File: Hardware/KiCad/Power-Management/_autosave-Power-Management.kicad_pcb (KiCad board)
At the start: 2 copper layers, 108 x 67 mm, 52 parts, among them IC1 RT9080-33GJ5, J1 Screw_Terminal_01x02, J2 Conn_01x06, J3 Screw_Terminal_01x02, K1 FINDER-36.11, Q1 BC817, T1 ZMPT101B, U1 STM32F401CCU6, U2 ACS758xCB-050B-PFF, U3 ESP-01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

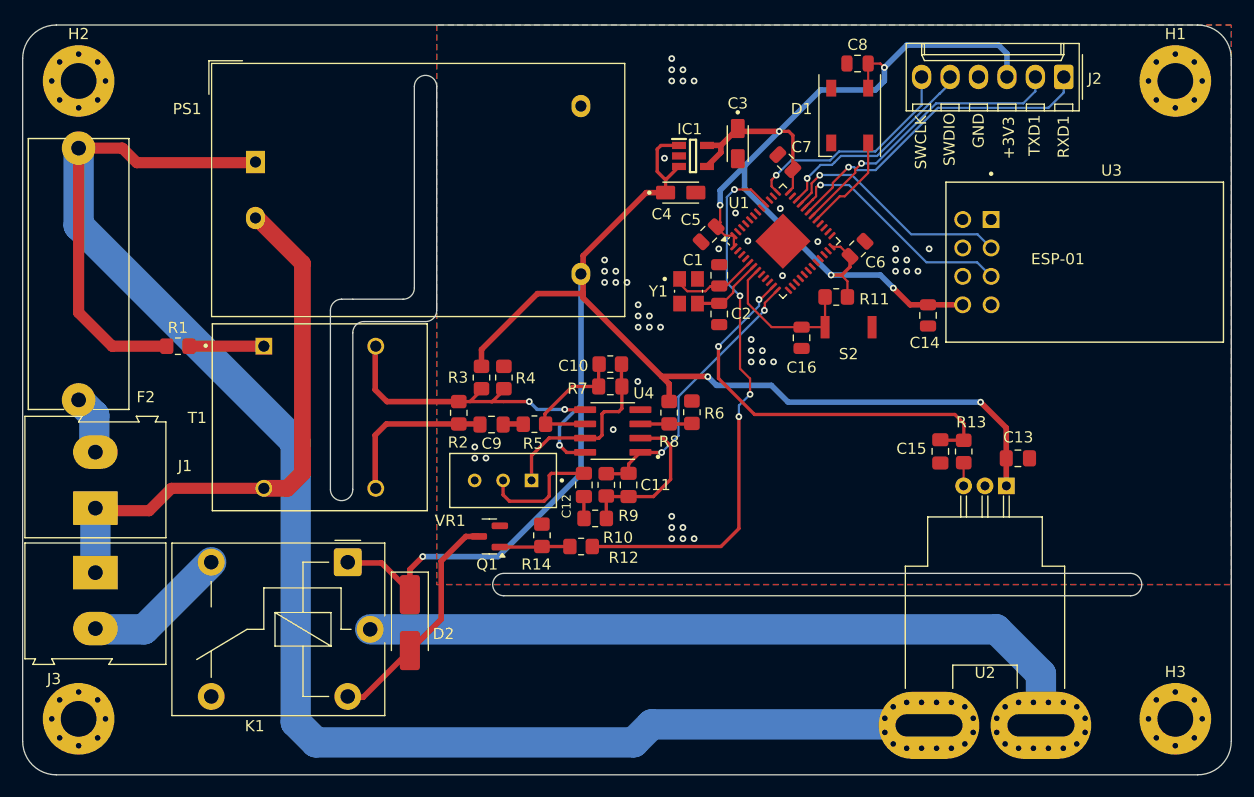
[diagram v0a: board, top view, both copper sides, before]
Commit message: refactor: exchange of STMF401 for F103
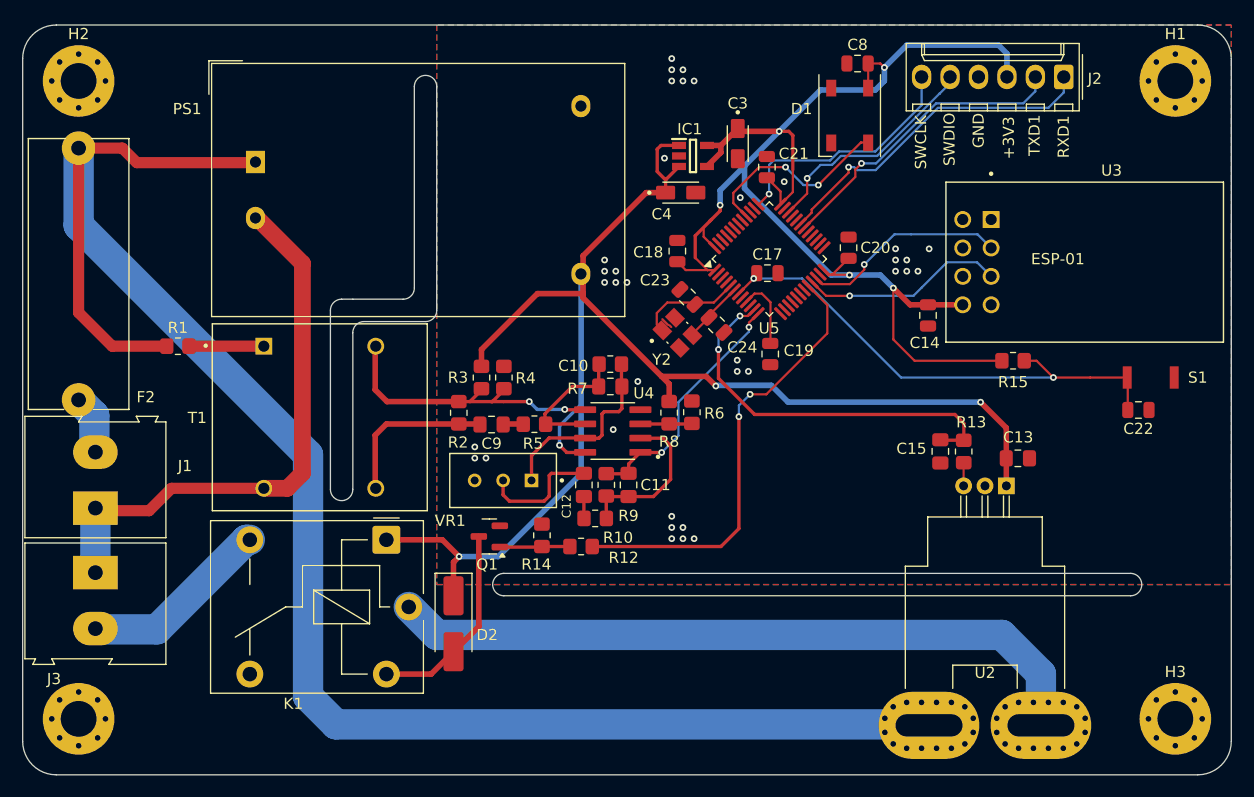
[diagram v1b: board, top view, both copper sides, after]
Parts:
- removed C1: 5pF, Capacitor_SMD:C_0805_2012Metric
- removed C16, C6: 100nF, Capacitor_SMD:C_0805_2012Metric
- removed C2, C7: 10pF, Capacitor_SMD:C_0805_2012Metric
- removed C5: 22uF 10V, Capacitor_SMD:C_0805_2012Metric
- removed R11: 10K, Resistor_SMD:R_0805_2012Metric_Pad1.20x1.40mm_HandSolder
- removed S2: SKRKAEE010, SKRKAEE010:SKRK
- removed U1: STM32F401CCU6, Package_DFN_QFN:QFN-48-1EP_7x7mm_P0.5mm_EP3.5x3.5mm
- removed Y1: 25Mhz, TSX-3225_25.0000MF10Z-W:XTAL_TSX-3225_25.0000MF10Z-W
- added C17: 100nF, Capacitor_SMD:C_0805_2012Metric, F.Cu at (188.6, 72.2)
- added C18: 100nF, Capacitor_SMD:C_0805_2012Metric, F.Cu at (180.5, 70.2)
- added C19: 10uF, Capacitor_SMD:C_0805_2012Metric, F.Cu at (188.8, 79.4)
- added C20: 100nF, Capacitor_SMD:C_0805_2012Metric, F.Cu at (195.8, 69.9)
- added C21: 100nF, Capacitor_SMD:C_0805_2012Metric, F.Cu at (188.5, 62.7)
- added C22: 100nF, Capacitor_SMD:C_0805_2012Metric, F.Cu at (221.7, 84.4)
- added C23: 10pF, Capacitor_SMD:C_0805_2012Metric, F.Cu at (181.4, 74.3)
- added C24: 10pF, Capacitor_SMD:C_0805_2012Metric, F.Cu at (184.0, 76.8)
- added R15: 10K, Resistor_SMD:R_0805_2012Metric_Pad1.20x1.40mm_HandSolder, F.Cu at (210.5, 80.0)
- added S1: SKRKAEE010, SKRKAEE010:SKRK, F.Cu at (222.8, 81.5)
- added U5: STM32F103C8Tx, Package_QFP:LQFP-48_7x7mm_P0.5mm, F.Cu at (188.7, 70.9)
- added Y2: 16Mhz, TSX-3225_25.0000MF10Z-W:XTAL_TSX-3225_25.0000MF10Z-W, F.Cu at (180.5, 77.5)
- moved K1 3.99 mm to (154.5, 96.0)
- moved D2 3.90 mm to (160.5, 103.5)
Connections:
- U3 pad 2: RXD6 -> RXD3
- U3 pad 3: TXD6 -> TXD3
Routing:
- net Net-(U5-NRST): track 0.00 -> 45.1 mm, vias 0 -> 2
- net +3V3: track 92.9 -> 124.1 mm
- net TXD6: track 21.5 -> 0.00 mm, vias 1 -> 0
- net RXD6: track 21.3 -> 0.00 mm, vias 1 -> 0
- net RXD3: track 0.00 -> 18.5 mm, vias 0 -> 1
- net TXD3: track 0.00 -> 18.3 mm, vias 0 -> 1
- net Net-(U1-NRST): track 13.8 -> 0.00 mm
- net Net-(U5-PD0): track 0.00 -> 9.22 mm
- net PIN_LED_RGB: track 9.06 -> 17.8 mm, vias 0 -> 2
- net PIN_RELAY: track 48.9 -> 40.3 mm, vias 4 -> 2
- net Net-(U1-PH0): track 8.00 -> 0.00 mm
- net Net-(U1-PH1): track 6.68 -> 0.00 mm
- net F/N-1 Borne: track 12.9 -> 17.1 mm
- net Net-(U5-PD1): track 0.00 -> 4.19 mm
- net +5V: track 137.3 -> 133.5 mm
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
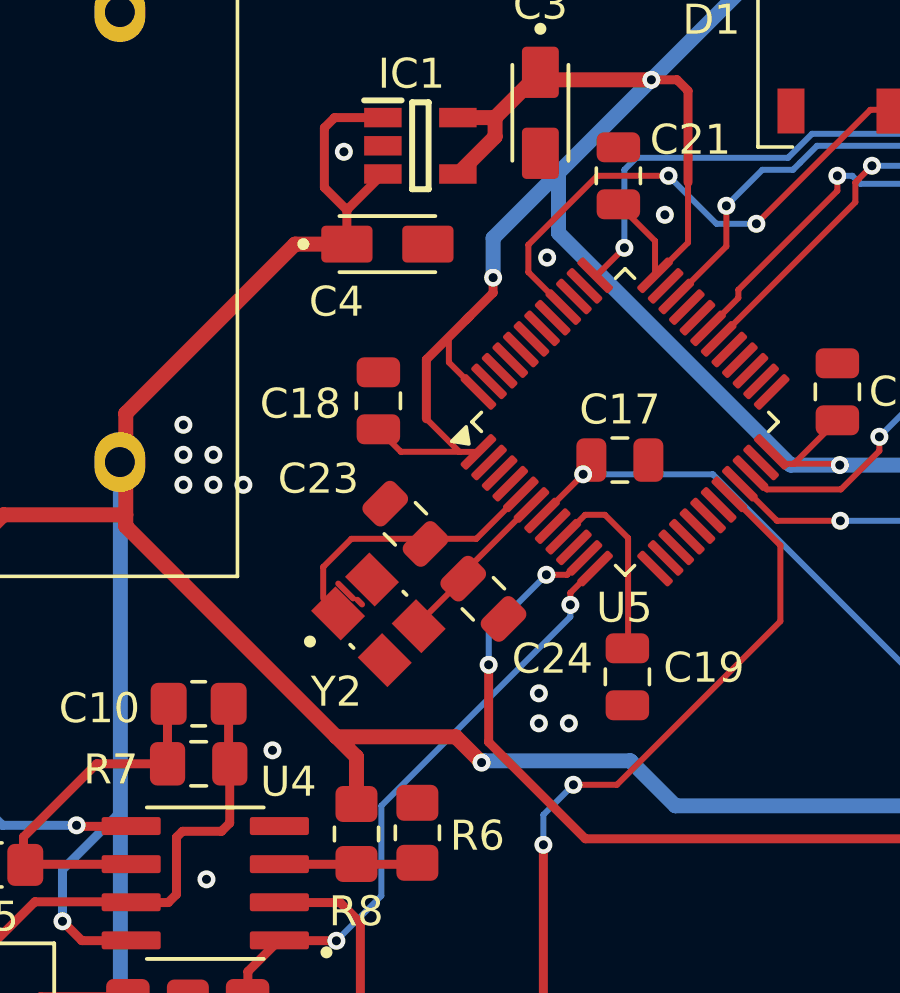
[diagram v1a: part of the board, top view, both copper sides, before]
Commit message: feat: footprint and step
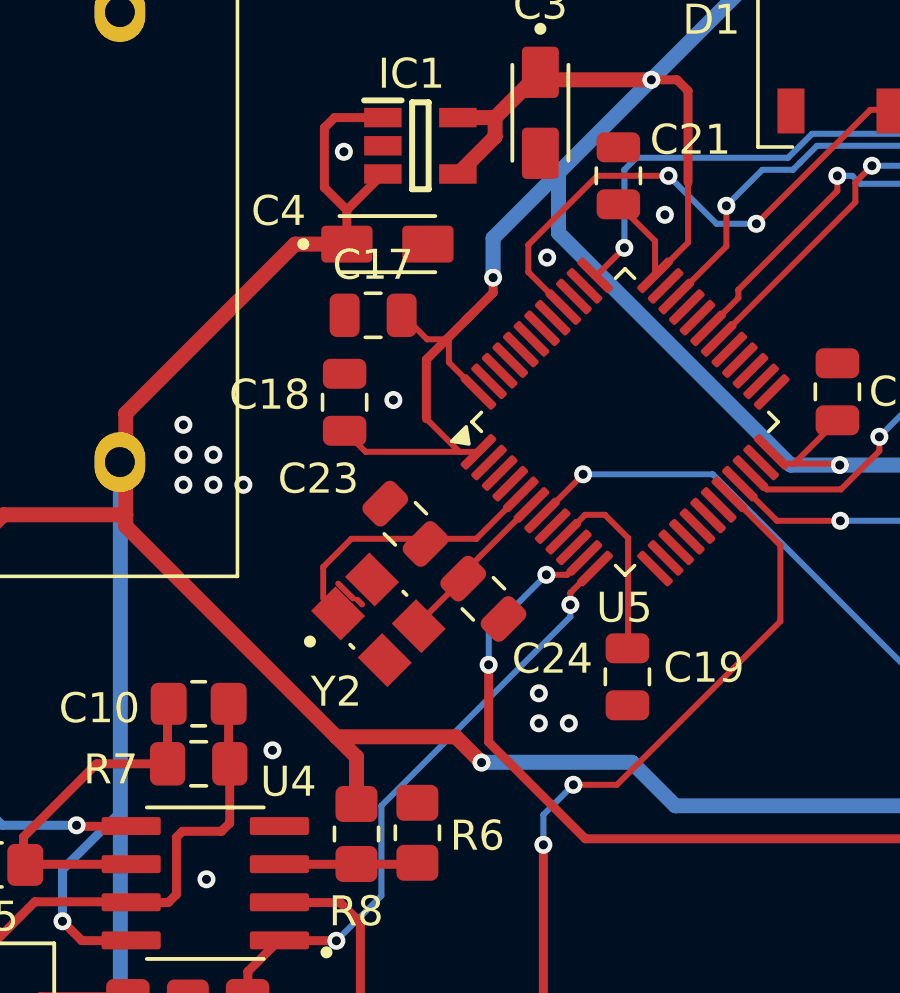
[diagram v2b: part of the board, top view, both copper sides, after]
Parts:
- moved C17 9.54 mm to (180.3, 67.3)
- moved C18 1.13 mm to (179.4, 70.2)
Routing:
- net +3V3: track 124.1 -> 127.0 mm
- net GND: vias 36 -> 37
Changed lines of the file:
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@@
 		(at 180.8 64.977)
 		(property "Reference" "C4"
-			(at -1.7 1.923 0)
+			(at -3.625 -1.102 0)
 			(layer "F.SilkS")
 			(effects
@@
 	(footprint "Capacitor_SMD:C_0805_2012Metric"
 		(layer "F.Cu")
-		(at 188.55 72.175)
+		(at 180.325 67.35)
 		(descr "Capacitor SMD 0805 (2012 Metric), square (rectangular) end terminal, IPC_7351 nominal, (Body size source: IPC-SM-782 page 76, https://www.pcb-3d.com/wordpress/wp-content/uploads/ipc-sm-782a_amendment_1_and_2.pdf, https://docs.google.com/spreadsheets/d/1BsfQQcO9C6DZCsRaXUlFlo91Tg2WpOkGARC1WS5S8t0/edit?usp=sharing), generated with kicad-footprint-generator")
 		(tags "capacitor")
@@
 	(footprint "Capacitor_SMD:C_0805_2012Metric"
 		(layer "F.Cu")
-		(at 180.5 70.2 -90)
+		(at 179.375 70.25 -90)
 		(descr "Capacitor SMD 0805 (2012 Metric), square (rectangular) end terminal, IPC_7351 nominal, (Body size source: IPC-SM-782 page 76, https://www.pcb-3d.com/wordpress/wp-content/uploads/ipc-sm-782a_amendment_1_and_2.pdf, https://docs.google.com/spreadsheets/d/1BsfQQcO9C6DZCsRaXUlFlo91Tg2WpOkGARC1WS5S8t0/edit?usp=sharing), generated with kicad-footprint-generator")
 		(tags "capacitor")
 		(property "Reference" "C18"
-			(at 0.1 2.6 180)
+			(at -0.25 2.5 180)
 			(layer "F.SilkS")
 			(effects
@@
 	)
 	(via
+		(at 181 70.175)
+		(size 0.6)
+		(drill 0.3)
+		(layers "F.Cu" "B.Cu")
+		(free yes)
+		(net 1)
+	)
+	(via
 		(at 180 94.9)
 		(size 0.6)
@@
 	)
 	(segment
+		(start 182.125 68.15)
+		(end 182.775 68.15)
+		(width 0.2)
+		(layer "F.Cu")
+		(net 2)
+	)
+	(segment
 		(start 183.425 67.5)
 		(end 184.3244 66.6006)
@@
 	)
 	(segment
+		(start 182.775 68.15)
+		(end 182.1 68.825)
+		(width 0.3)
+		(layer "F.Cu")
+		(net 2)
+	)
+	(segment
 		(start 182.1 70.8)
 		(end 183.20245 71.90245)
@@
 	)
 	(segment
+		(start 183.2 71.9)
+		(end 183.20245 71.90245)
+		(width 0.2)
+		(layer "F.Cu")
+		(net 2)
+	)
+	(segment
 		(start 184.39 61.4)
 		(end 183.15 62.64)
@@
 	)
 	(segment
+		(start 181.325 67.35)
+		(end 182.125 68.15)
+		(width 0.2)
+		(layer "F.Cu")
+		(net 2)
+	)
+	(segment
 		(start 193.610878 71.90245)
 		(end 194.008428 72.3)
@@
 	)
 	(segment
+		(start 180.075 71.9)
+		(end 183.2 71.9)
+		(width 0.2)
+		(layer "F.Cu")
+		(net 2)
+	)
+	(segment
 		(start 190.821751 62.921751)
 		(end 190.821751 64.928249)
@@
 	)
 	(segment
+		(start 179.375 71.2)
+		(end 180.075 71.9)
+		(width 0.2)
+		(layer "F.Cu")
+		(net 2)
+	)
+	(segment
 		(start 209.5 80)
 		(end 201.7 80)
@@
 	)
 	(segment
-		(start 180.5 71.15)
-		(end 181.25 71.9)
-		(width 0.2)
-		(layer "F.Cu")
-		(net 2)
-	)
-	(segment
 		(start 197.55417 55.63857)
 		(end 197.55317 55.63957)
@@
 	)
 	(segment
-		(start 181.25 71.9)
-		(end 183.2 71.9)
-		(width 0.2)
-		(layer "F.Cu")
-		(net 2)
-	)
-	(segment
 		(start 201.3 75)
 		(end 199.8 73.5)
@@
 	)
 	(segment
-		(start 183.2 71.9)
-		(end 183.20245 71.90245)
-		(width 0.2)
-		(layer "F.Cu")
-		(net 2)
-	)
-	(segment
 		(start 183.5375 67.3875)
-		(end 182.1 68.825)
+		(end 182.775 68.15)
 		(width 0.3)
 		(layer "F.Cu")
@@
 	)
 	(segment
-		(start 183.94038 82.25962)
-		(end 183.08076 81.4)
+		(start 183.08076 81.4)
+		(end 179.1 81.4)
 		(width 0.5)
 		(layer "F.Cu")
@@
 	)
 	(segment
-		(start 183.08076 81.4)
-		(end 179.1 81.4)
-		(width 0.5)
-		(layer "F.Cu")
-		(net 5)
-	)
-	(segment
 		(start 179.77 82.07)
 		(end 179.77 83.65)
@@
 		(net 5)
 	)
+	(segment
+		(start 183.94038 82.25962)
+		(end 183.08076 81.4)
+		(width 0.5)
+		(layer "F.Cu")
+		(net 5)
+	)
 	(via
 		(at 161 97.5)
@@
 	)
 	(segment
-		(start 164.5 97.5)
-		(end 161 97.5)
+		(start 188.95 82.25)
+		(end 190.4 83.7)
 		(width 0.5)
 		(layer "B.Cu")
@@
 	)
 	(segment
-		(start 171.9 72.26)
-		(end 171.8825 72.2425)
+		(start 183.95 82.25)
+		(end 188.95 82.25)
 		(width 0.5)
 		(layer "B.Cu")
@@
 	)
 	(segment
-		(start 188.9 82.2)
-		(end 190.4 83.7)
+		(start 164.5 97.5)
+		(end 161 97.5)
 		(width 0.5)
 		(layer "B.Cu")
@@
 	)
 	(segment
-		(start 171.8 84)
-		(end 169.97 85.83)
-		(width 0.3)
-		(layer "B.Cu")
-		(net 5)
-	)
-	(segment
 		(start 190.4 83.7)
 		(end 207.6 83.7)
@@
 	)
 	(segment
-		(start 169.97 85.83)
-		(end 169.97 87.55)
-		(width 0.3)
+		(start 171.9 72.26)
+		(end 171.8825 72.2425)
+		(width 0.5)
 		(layer "B.Cu")
 		(net 5)
@@
 	(segment
 		(start 183.94038 82.25962)
-		(end 184 82.2)
+		(end 183.95 82.25)
 		(width 0.5)
 		(layer "B.Cu")
@@
 	)
 	(segment
-		(start 184 82.2)
-		(end 188.9 82.2)
-		(width 0.5)
+		(start 171.8 84)
+		(end 169.97 85.83)
+		(width 0.3)
+		(layer "B.Cu")
+		(net 5)
+	)
+	(segment
+		(start 169.97 85.83)
+		(end 169.97 87.55)
+		(width 0.3)
 		(layer "B.Cu")
 		(net 5)

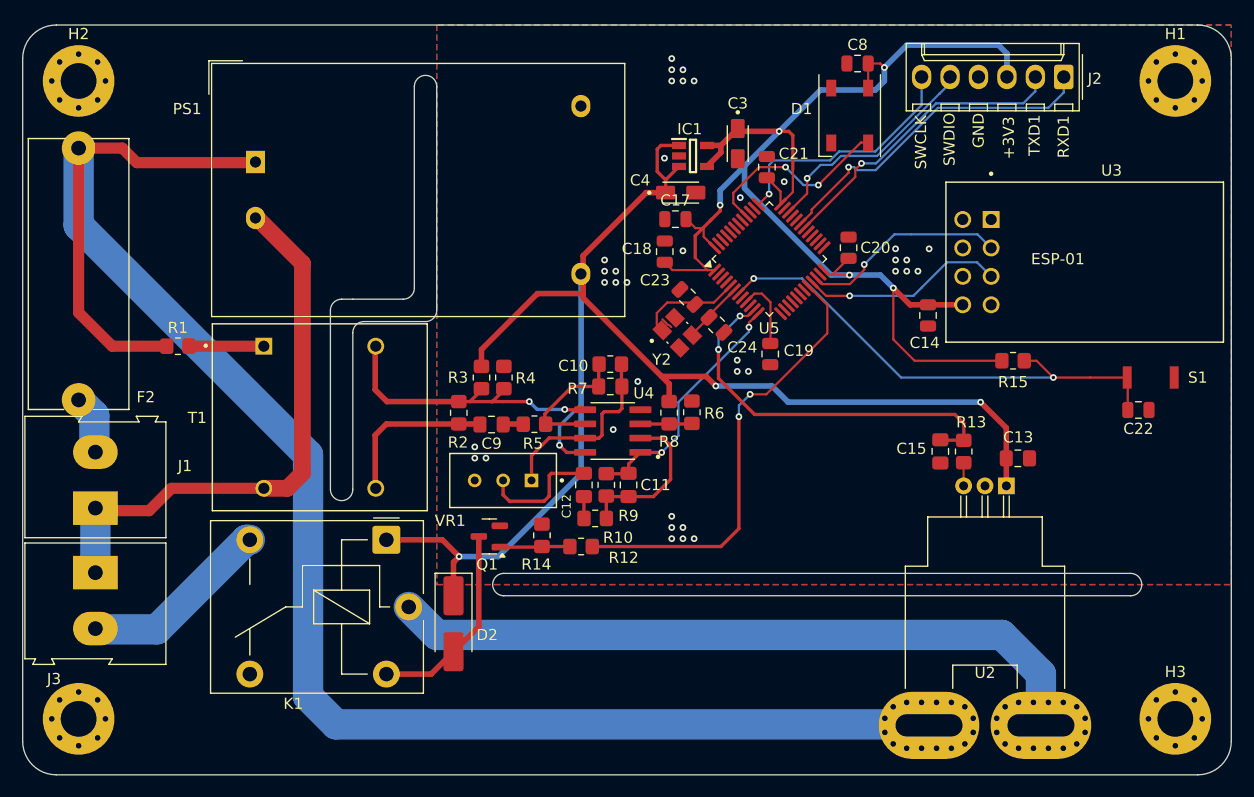
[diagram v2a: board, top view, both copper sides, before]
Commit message: feat: text and icons in silkscreen
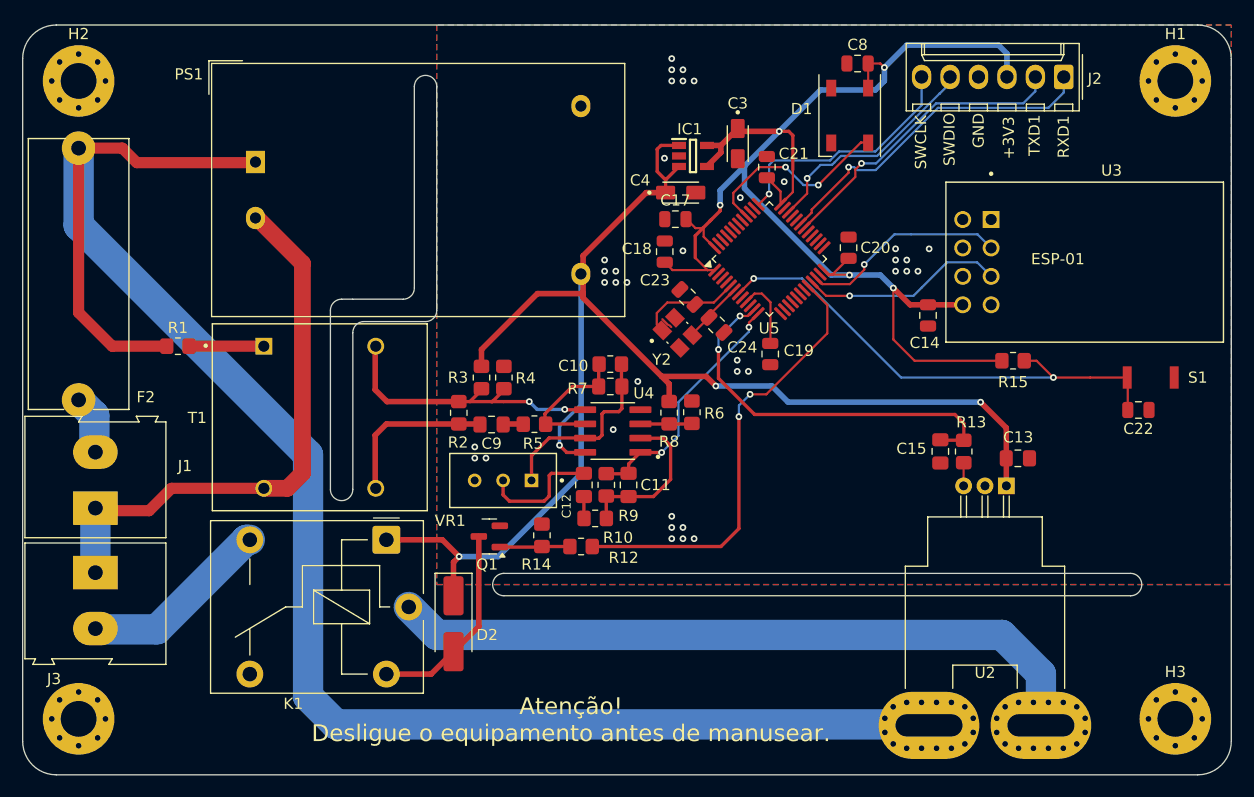
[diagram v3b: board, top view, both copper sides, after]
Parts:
- added G***: LOGO, Silkscreen images:Attention_high_voltage, B.Cu at (137.0, 57.0)
- added G***: LOGO, Silkscreen images:Attention_high_voltage, B.Cu at (137.0, 110.0)
- added G***: LOGO, Silkscreen images:Attention_high_voltage, B.Cu at (137.0, 86.0)
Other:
- board text added: "Atenção! Desligue o equipamento antes de manusear."
